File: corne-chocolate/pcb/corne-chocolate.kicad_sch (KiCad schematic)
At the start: 28 parts, among them J1 MJ-4PP-9, J2 nice!view, J3 Battery, J4 Battery, SW21 1.5U, SW22 SW_PUSH, SW23 SW_SPDT, SW24 SW_SPDT, U1 ProMicro

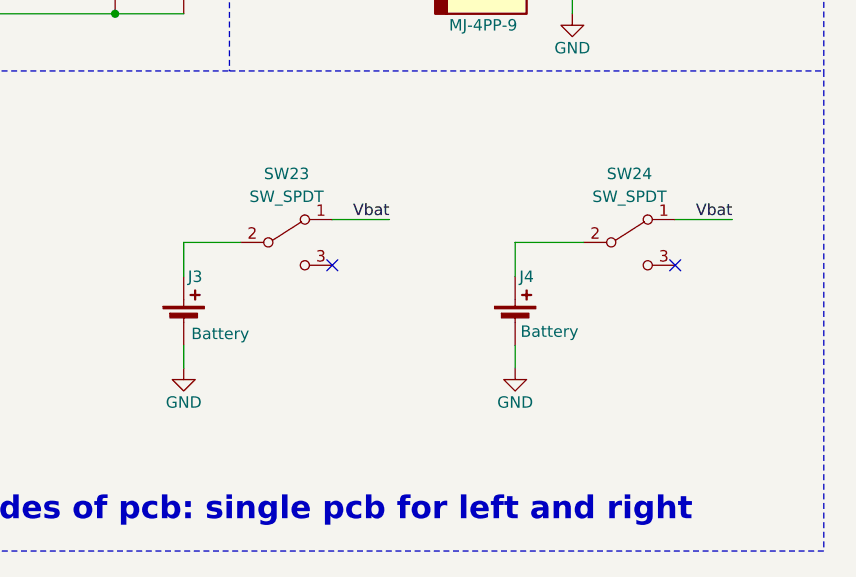
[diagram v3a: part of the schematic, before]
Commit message: pcb change on/off switch
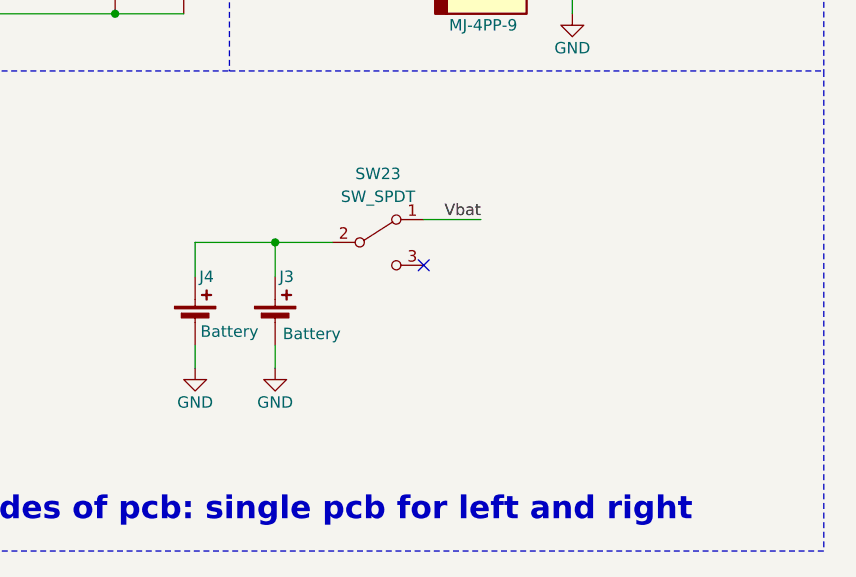
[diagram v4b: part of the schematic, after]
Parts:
- removed SW24: SW_SPDT, Button_Switch_SMD:SW_SPDT_PCM12, symbol Switch:SW_SPDT
- SW23: footprint Button_Switch_SMD:SW_SPDT_PCM12 -> corne-chocolate:ECE_ESP2010
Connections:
- net at J4.1 (+): now also J3.1 (+), SW23.2 (B)
- no-connect marks 8 -> 7
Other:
- moved on the sheet: J3, J4, SW23
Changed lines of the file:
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@@
 	)
 	(junction
+		(at 219.71 127)
+		(diameter 0)
+		(color 0 0 0 0)
+	)
+	(junction
 		(at 73.66 34.29)
 		(diameter 0)
@@
 	)
 	(no_connect
-		(at 264.16 129.54)
-	)
-	(no_connect
-		(at 226.06 129.54)
+		(at 236.22 129.54)
 	)
 	(no_connect
@@
 	(wire
 		(pts
-			(xy 246.38 138.43) (xy 246.38 140.97)
+			(xy 210.82 138.43) (xy 210.82 140.97)
 		)
 		(stroke
@@
 	(wire
 		(pts
-			(xy 254 127) (xy 246.38 127)
-		)
-		(stroke
-			(width 0)
-			(type default)
-		)
-	)
-	(wire
-		(pts
 			(xy 90.17 81.28) (xy 93.98 81.28)
 		)
@@
 	(wire
 		(pts
-			(xy 209.55 127) (xy 209.55 130.81)
+			(xy 219.71 127) (xy 219.71 130.81)
 		)
 		(stroke
@@
 	(wire
 		(pts
+			(xy 210.82 127) (xy 219.71 127)
+		)
+		(stroke
+			(width 0)
+			(type default)
+		)
+	)
+	(wire
+		(pts
 			(xy 129.54 34.29) (xy 129.54 39.37)
 		)
@@
 	(wire
 		(pts
-			(xy 209.55 138.43) (xy 209.55 140.97)
+			(xy 219.71 138.43) (xy 219.71 140.97)
 		)
 		(stroke
@@
 	(wire
 		(pts
-			(xy 264.16 124.46) (xy 270.51 124.46)
-		)
-		(stroke
-			(width 0)
-			(type default)
-		)
-	)
-	(wire
-		(pts
 			(xy 46.99 69.85) (xy 73.66 69.85)
 		)
@@
 	(wire
 		(pts
-			(xy 246.38 127) (xy 246.38 130.81)
+			(xy 210.82 127) (xy 210.82 130.81)
 		)
 		(stroke
@@
 	(wire
 		(pts
-			(xy 215.9 127) (xy 209.55 127)
+			(xy 226.06 127) (xy 219.71 127)
 		)
 		(stroke
@@
 	(wire
 		(pts
-			(xy 226.06 124.46) (xy 232.41 124.46)
+			(xy 236.22 124.46) (xy 242.57 124.46)
 		)
 		(stroke
@@
 	)
 	(label "Vbat"
-		(at 232.41 124.46 180)
+		(at 242.57 124.46 180)
 		(effects
 			(font
@@
 		)
 	)
-	(label "Vbat"
-		(at 270.51 124.46 180)
-		(effects
-			(font
-				(size 1.27 1.27)
-			)
-			(justify right bottom)
-		)
-	)
 	(label "L1"
 		(at 113.03 157.48 0)
@@
 	(symbol
 		(lib_id "Device:Battery_Cell")
-		(at 246.38 135.89 0)
+		(at 210.82 135.89 0)
 		(unit 1)
 		(exclude_from_sim no)
@@
 		(dnp no)
 		(property "Reference" "J4"
-			(at 247.65 130.81 0)
+			(at 212.09 130.81 0)
 			(effects
 				(font
@@
 		)
 		(property "Value" "Battery"
-			(at 250.19 136.906 0)
+			(at 214.63 136.906 0)
 			(effects
 				(font
@@
 		)
 		(property "Footprint" "Connector_JST:JST_PH_S2B-PH-SM4-TB_1x02-1MP_P2.00mm_Horizontal"
-			(at 246.38 134.366 90)
+			(at 210.82 134.366 90)
 			(effects
 				(font
@@
 		)
 		(property "Datasheet" "~"
-			(at 246.38 134.366 90)
+			(at 210.82 134.366 90)
 			(effects
 				(font
@@
 		)
 		(property "Description" "Single-cell battery"
-			(at 246.38 135.89 0)
+			(at 210.82 135.89 0)
 			(effects
 				(font
@@
 	(symbol
 		(lib_id "Device:Battery_Cell")
-		(at 209.55 135.89 0)
+		(at 219.71 135.89 0)
 		(unit 1)
 		(exclude_from_sim no)
@@
 		(dnp no)
 		(property "Reference" "J3"
-			(at 210.82 130.81 0)
+			(at 220.98 130.81 0)
 			(effects
 				(font
@@
 		)
 		(property "Value" "Battery"
-			(at 213.614 137.16 0)
+			(at 223.774 137.16 0)
 			(effects
 				(font
@@
 		)
 		(property "Footprint" "Connector_JST:JST_PH_S2B-PH-SM4-TB_1x02-1MP_P2.00mm_Horizontal"
-			(at 209.55 134.366 90)
+			(at 219.71 134.366 90)
 			(effects
 				(font
@@
 		)
 		(property "Datasheet" "~"
-			(at 209.55 134.366 90)
+			(at 219.71 134.366 90)
 			(effects
 				(font
@@
 		)
 		(property "Description" "Single-cell battery"
-			(at 209.55 135.89 0)
+			(at 219.71 135.89 0)
 			(effects
 				(font
@@
 	(symbol
 		(lib_id "power:GND")
-		(at 209.55 140.97 0)
+		(at 219.71 140.97 0)
 		(unit 1)
 		(exclude_from_sim no)
@@
 		(dnp no)
 		(property "Reference" "#PWR014"
-			(at 209.55 147.32 0)
+			(at 219.71 147.32 0)
 			(effects
 				(font
@@
 		)
 		(property "Value" "GND"
-			(at 209.55 144.78 0)
+			(at 219.71 144.78 0)
 			(effects
 				(font
@@
 		)
 		(property "Footprint" ""
-			(at 209.55 140.97 0)
+			(at 219.71 140.97 0)
 			(effects
 				(font
@@
 		)
 		(property "Datasheet" ""
-			(at 209.55 140.97 0)
+			(at 219.71 140.97 0)
 			(effects
 				(font
@@
 		)
 		(property "Description" ""
-			(at 209.55 140.97 0)
+			(at 219.71 140.97 0)
 			(effects
 				(font
@@
 	)
 	(symbol
-		(lib_id "Switch:SW_SPDT")
-		(at 259.08 127 0)
-		(unit 1)
-		(exclude_from_sim no)
-		(in_bom yes)
-		(on_board yes)
-		(dnp no)
-		(fields_autoplaced yes)
-		(property "Reference" "SW24"
-			(at 259.08 119.38 0)
-			(effects
-				(font
-					(size 1.27 1.27)
-				)
-			)
-		)
-		(property "Value" "SW_SPDT"
-			(at 259.08 121.92 0)
-			(effects
-				(font
-					(size 1.27 1.27)
-				)
-			)
-		)
-		(property "Footprint" "Button_Switch_SMD:SW_SPDT_PCM12"
-			(at 259.08 127 0)
-			(effects
-				(font
-					(size 1.27 1.27)
-				)
-				(hide yes)
-			)
-		)
-		(property "Datasheet" "~"
-			(at 259.08 127 0)
-			(effects
-				(font
-					(size 1.27 1.27)
-				)
-				(hide yes)
-			)
-		)
-		(property "Description" ""
-			(at 259.08 127 0)
-			(effects
-				(font
-					(size 1.27 1.27)
-				)
-			)
-		)
-		(pin "1"
-		)
-		(pin "2"
-		)
-		(pin "3"
-		)
-		(instances
-			(project "corne-chocolate"
-				(path "/b2404ab0-025a-473e-9fbb-0abc932972cf"
-					(reference "SW24")
-					(unit 1)
-				)
-			)
-		)
-	)
-	(symbol
 		(lib_id "power:GND")
 		(at 53.34 165.1 0)
@@
 	(symbol
 		(lib_id "Switch:SW_SPDT")
-		(at 220.98 127 0)
+		(at 231.14 127 0)
 		(unit 1)
 		(exclude_from_sim no)
@@
 		(fields_autoplaced yes)
 		(property "Reference" "SW23"
-			(at 220.98 119.38 0)
+			(at 231.14 119.38 0)
 			(effects
 				(font
@@
 		)
 		(property "Value" "SW_SPDT"
-			(at 220.98 121.92 0)
+			(at 231.14 121.92 0)
 			(effects
 				(font
@@
 			)
 		)
-		(property "Footprint" "Button_Switch_SMD:SW_SPDT_PCM12"
-			(at 220.98 127 0)
+		(property "Footprint" "corne-chocolate:ECE_ESP2010"
+			(at 231.14 127 0)
 			(effects
 				(font
@@
 		)
 		(property "Datasheet" "~"
-			(at 220.98 127 0)
+			(at 231.14 127 0)
 			(effects
 				(font
@@
 		)
 		(property "Description" ""
-			(at 220.98 127 0)
+			(at 231.14 127 0)
 			(effects
 				(font
@@
 	(symbol
 		(lib_id "power:GND")
-		(at 246.38 140.97 0)
+		(at 210.82 140.97 0)
 		(unit 1)
 		(exclude_from_sim no)
@@
 		(dnp no)
 		(property "Reference" "#PWR015"
-			(at 246.38 147.32 0)
+			(at 210.82 147.32 0)
 			(effects
 				(font
@@
 		)
 		(property "Value" "GND"
-			(at 246.38 144.78 0)
+			(at 210.82 144.78 0)
 			(effects
 				(font
@@
 		)
 		(property "Footprint" ""
-			(at 246.38 140.97 0)
+			(at 210.82 140.97 0)
 			(effects
 				(font
@@
 		)
 		(property "Datasheet" ""
-			(at 246.38 140.97 0)
+			(at 210.82 140.97 0)
 			(effects
 				(font
@@
 		)
 		(property "Description" ""
-			(at 246.38 140.97 0)
+			(at 210.82 140.97 0)
 			(effects
 				(font

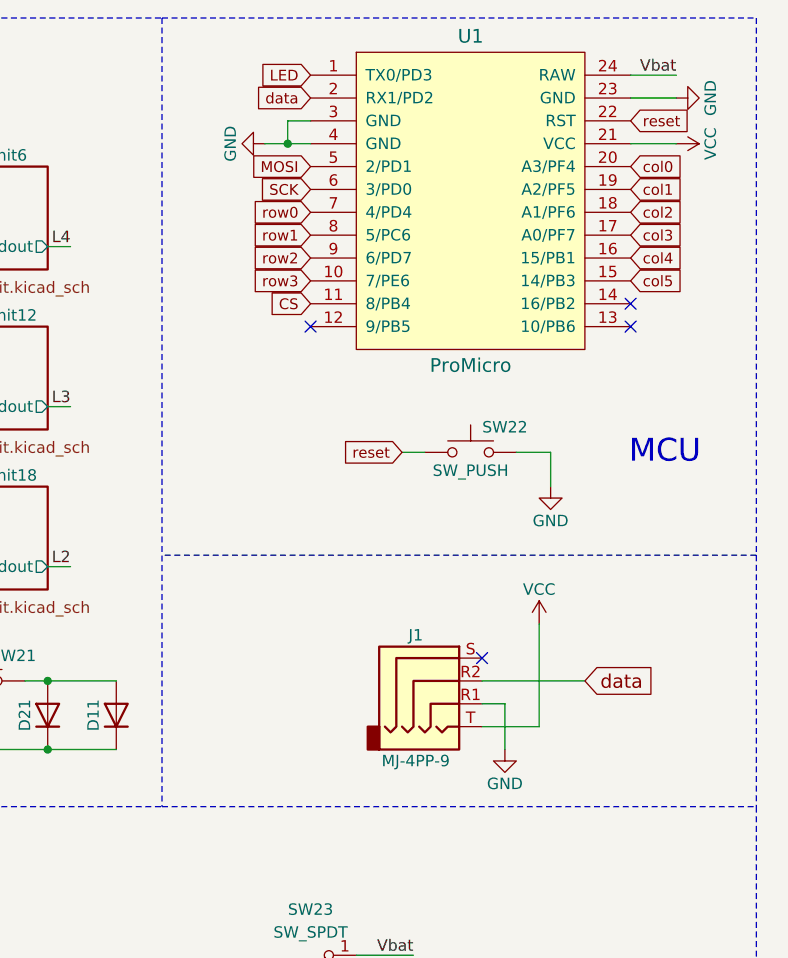
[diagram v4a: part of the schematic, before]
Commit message: pcb remove TRRS
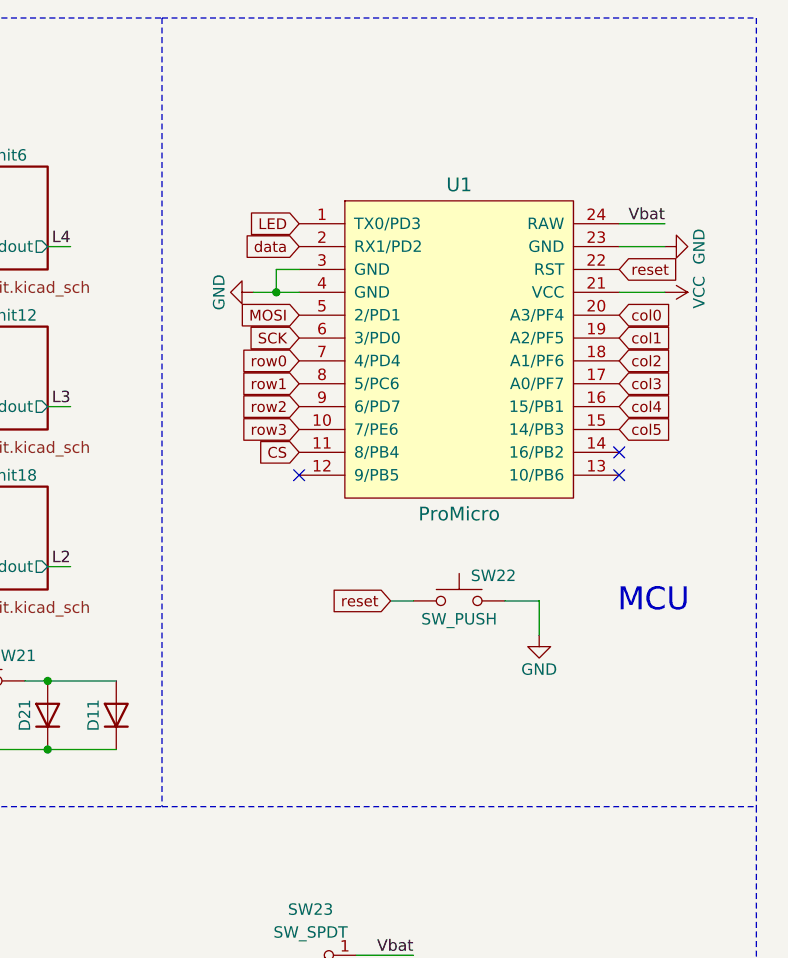
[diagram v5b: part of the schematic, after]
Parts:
- removed J1: MJ-4PP-9, corne-chocolate:MJ-4PP-9, symbol Connector_Audio:AudioJack4
- LED21, LED22, LED23, LED24, LED25, LED26, LED27: footprint LED_SMD:LED_SK6812MINI_PLCC4_3.5x3.5mm_P1.75mm -> corne-chocolate:SK6812MINI_underglow_rev
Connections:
- no-connect marks 7 -> 6
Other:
- moved on the sheet: SW22, U1

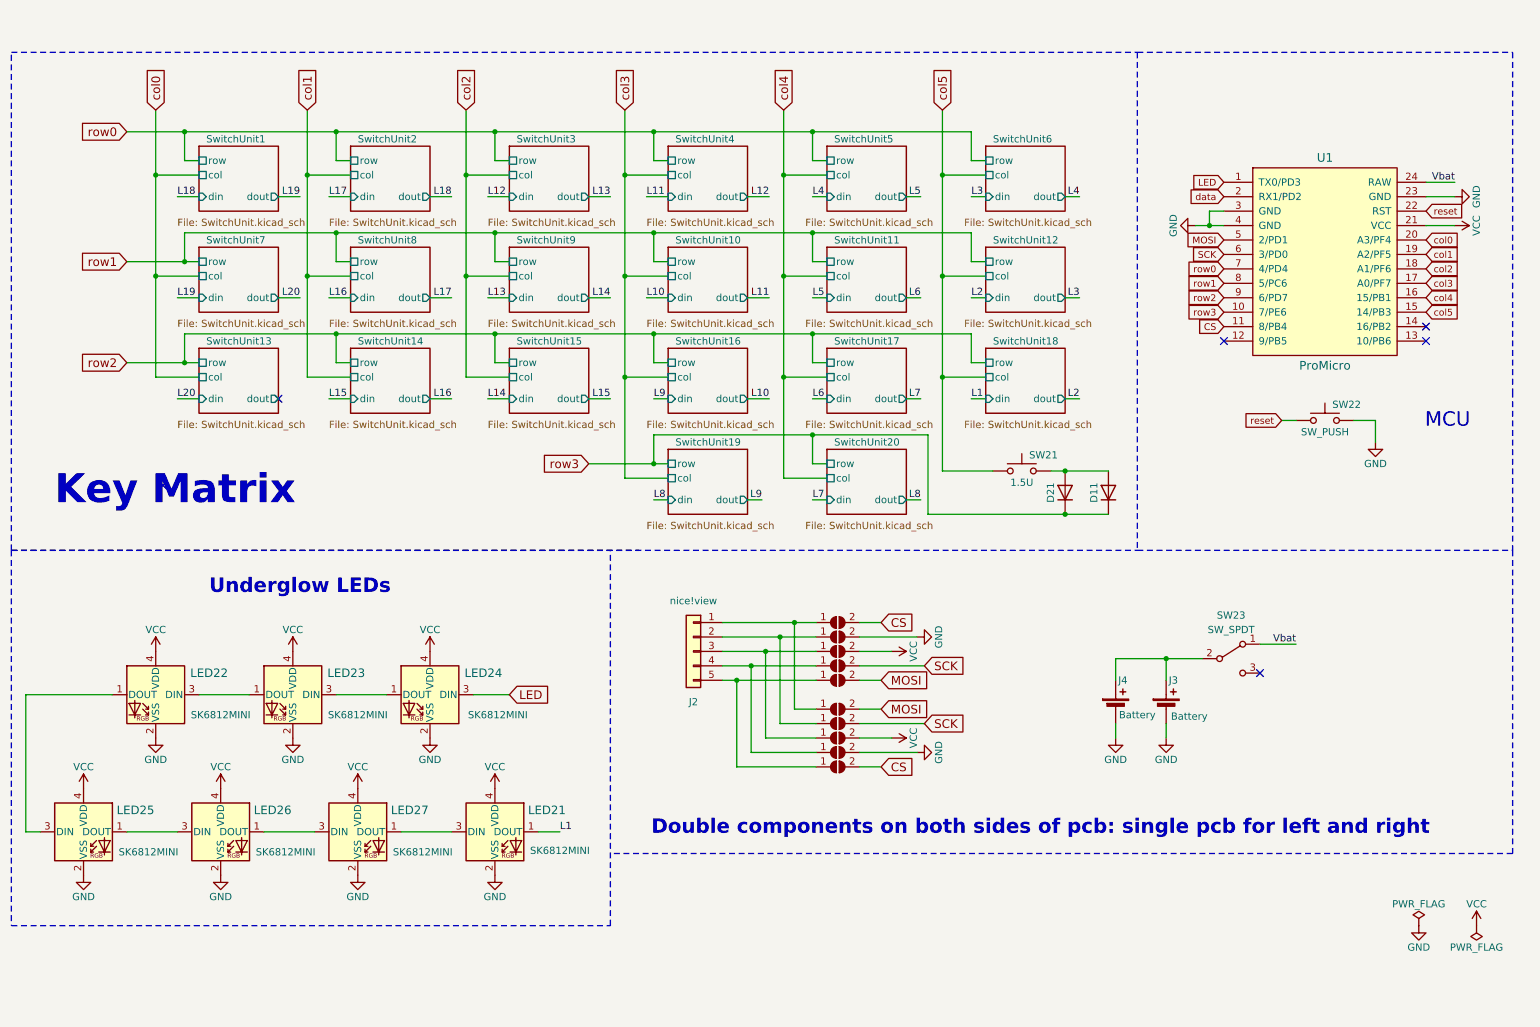
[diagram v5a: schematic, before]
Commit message: pcb remove underglow LEDs
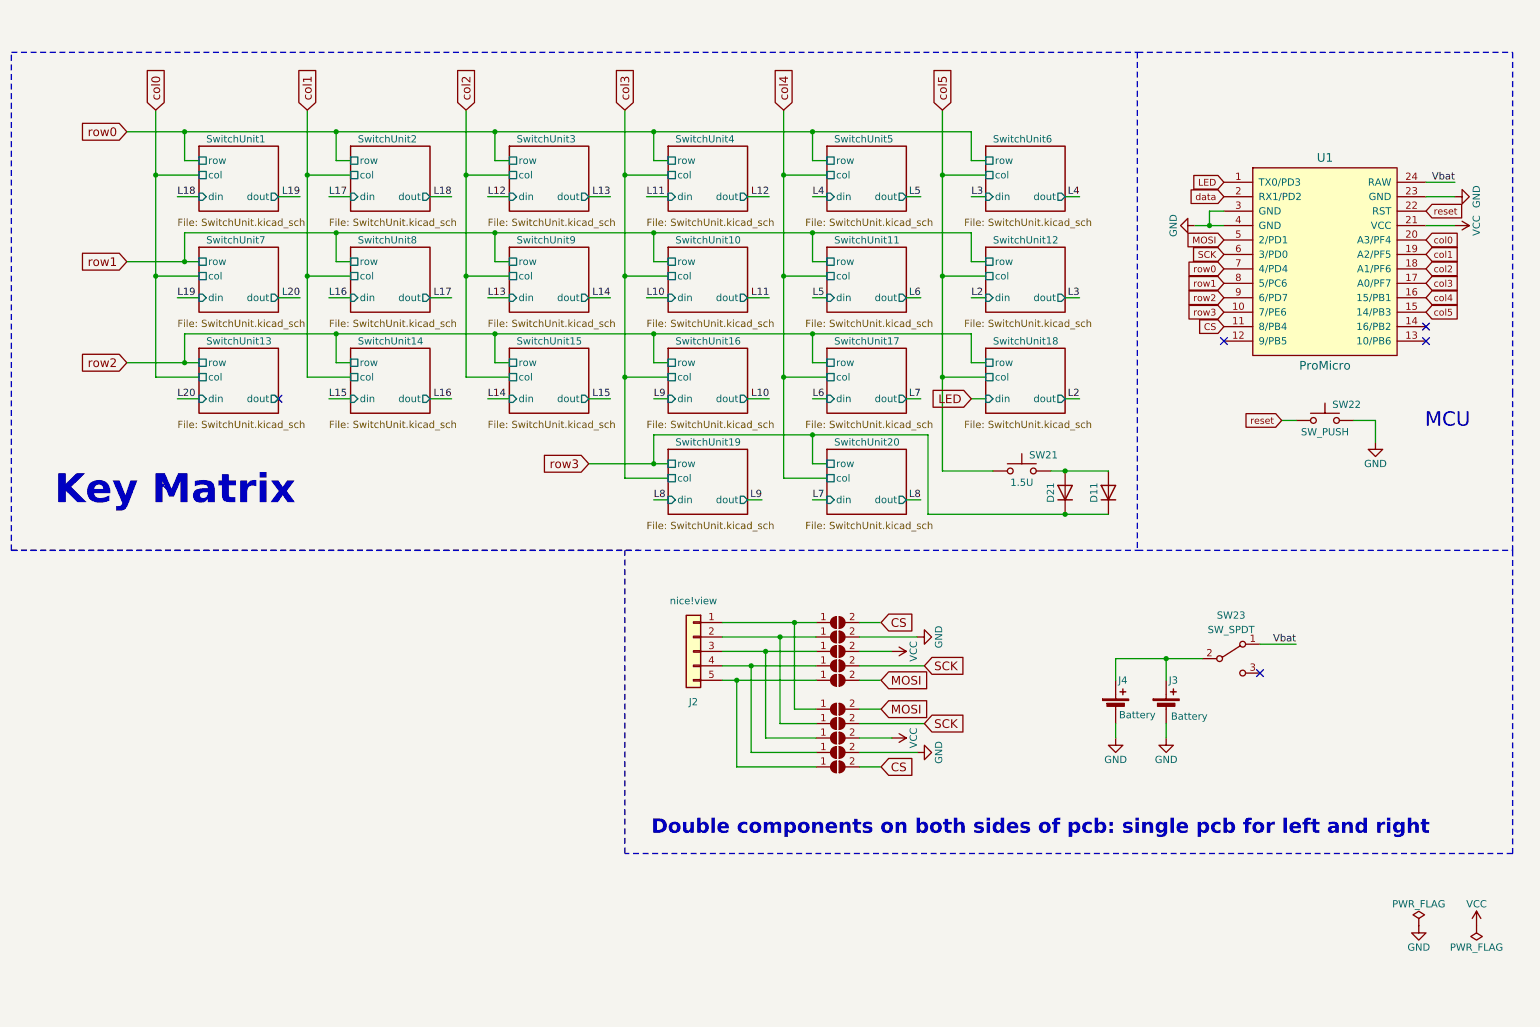
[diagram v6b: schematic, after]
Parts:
- removed LED21, LED22, LED23, LED24, LED25, LED26, LED27: SK6812MINI, corne-chocolate:SK6812MINI_underglow_rev, symbol LED:SK6812MINI
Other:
- note removed: "Underglow LEDs"
